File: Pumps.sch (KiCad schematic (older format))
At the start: 4 parts, among them Q1 TIP122

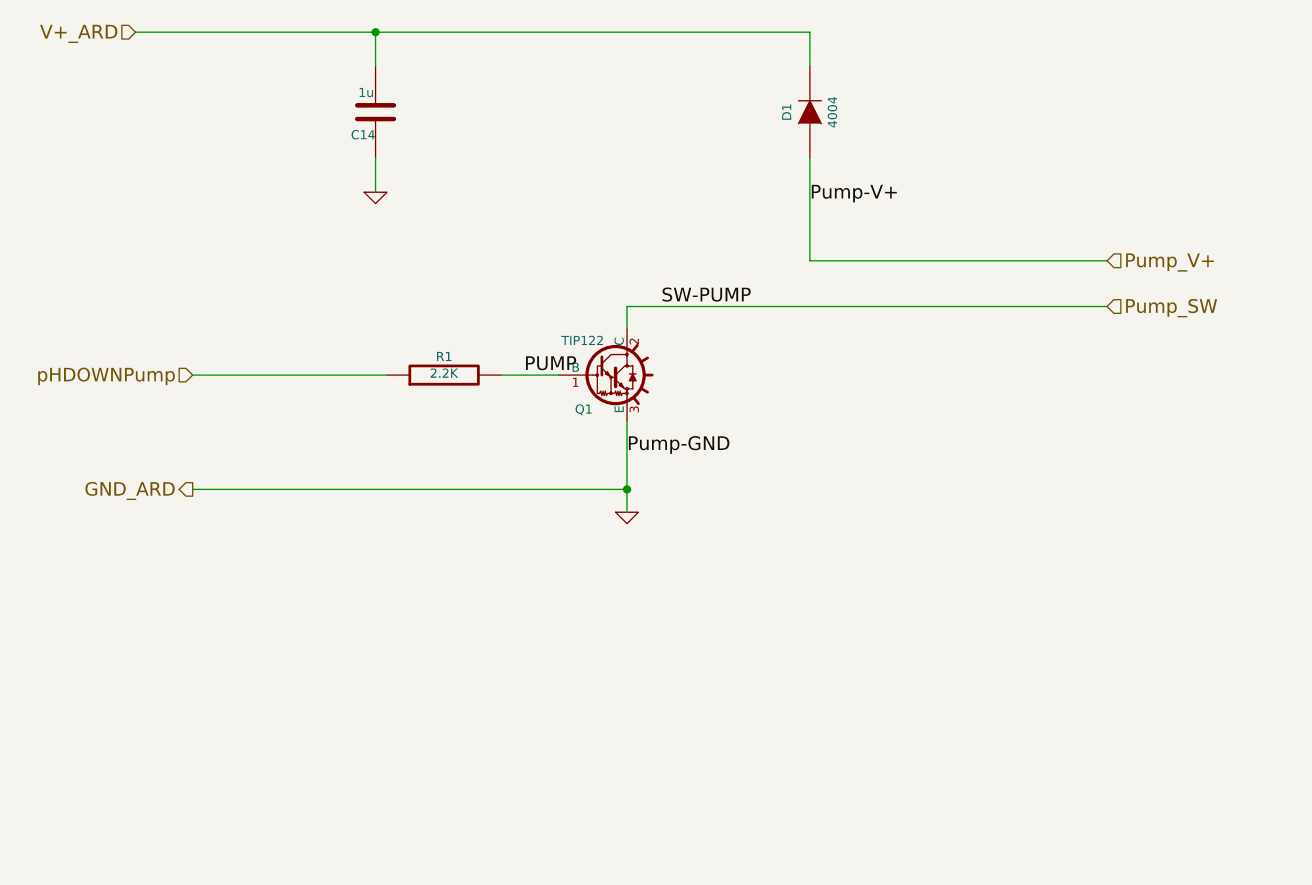
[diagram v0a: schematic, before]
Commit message: added 2nd pump in circuit to accomodate pH UP
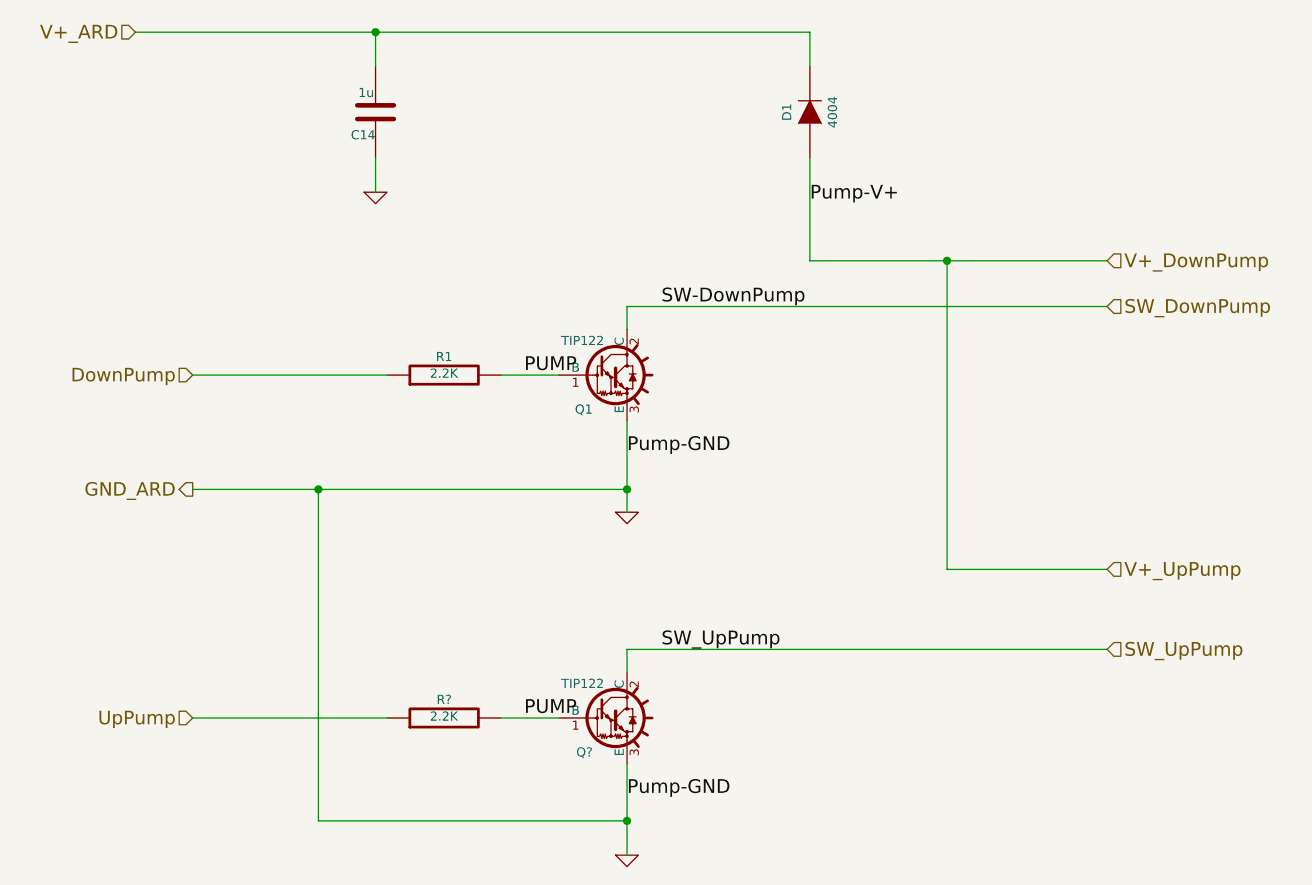
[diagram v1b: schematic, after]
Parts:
- added Q?: TIP122, TO220, symbol TIP120
- added R?: 2.2K, ~, symbol R
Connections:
- net GND: now also Q?.3 (E)
- net PUMP: now also Q?.1 (B), R?.2
- net Pump_SW renamed SW_DownPump
- net Pump_V+ renamed V+_DownPump
- net pHDOWNPump renamed DownPump
- new net SW_UpPump: Q?.2 (C)
- new net UpPump: R?.1
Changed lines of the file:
@@
 $Descr A4 11693 8268
 encoding utf-8
-Sheet 6 7
+Sheet 7 7
 Title ""
-Date "11 aug 2014"
+Date "12 aug 2014"
 Rev ""
 Comp ""
@@
 	4700 1150 4700 1300
 Text HLabel 2000 2650 0    59   Input ~ 0
-pHDOWNPump
+DownPump
 $Comp
 L GND #PWR12
@@
 	1750 1150 4700 1150
 Text Label 4050 2350 0    60   ~ 0
-SW-PUMP
+SW-DownPump
 Text Label 4700 1900 0    60   ~ 0
 Pump-V+
@@
 Pump-GND
 Text HLabel 6000 2150 2    60   Input ~ 0
-Pump_V+
+V+_DownPump
 Text HLabel 6000 2350 2    60   Input ~ 0
-Pump_SW
+SW_DownPump
+$Comp
+L TIP120 Q?
+U 1 1 53EA6E0F
+P 3800 4150
+F 0 "Q?" H 3750 4000 40  0000 R CNN
+F 1 "TIP122" H 3800 4300 40  0000 R CNN
+F 2 "TO220" H 3680 4255 29  0001 C CNN
+F 3 "~" H 3800 4150 60  0000 C CNN
+	1    3800 4150
+	1    0    0    -1
+$EndComp
+$Comp
+L R R?
+U 1 1 53EA6E15
+P 3100 4150
+F 0 "R?" V 3180 4150 40  0000 C CNN
+F 1 "2.2K" V 3107 4151 40  0000 C CNN
+F 2 "~" V 3030 4150 30  0000 C CNN
+F 3 "~" H 3100 4150 30  0000 C CNN
+	1    3100 4150
+	0    -1   -1   0
+$EndComp
+Wire Wire Line
+	3350 4150 3600 4150
+Wire Wire Line
+	2000 4150 2850 4150
+Text HLabel 2000 4150 0    59   Input ~ 0
+UpPump
+$Comp
+L GND #PWR?
+U 1 1 53EA6E1E
+P 3900 4750
+F 0 "#PWR?" H 3900 4750 30  0001 C CNN
+F 1 "GND" H 3900 4680 30  0001 C CNN
+F 2 "" H 3900 4750 60  0000 C CNN
+F 3 "" H 3900 4750 60  0000 C CNN
+	1    3900 4750
+	1    0    0    -1
+$EndComp
+Wire Wire Line
+	3900 3850 6000 3850
+Wire Wire Line
+	3900 3850 3900 3950
+Text Label 4050 3850 0    60   ~ 0
+SW_UpPump
+Text Label 3450 4150 0    60   ~ 0
+PUMP
+Wire Wire Line
+	3900 4350 3900 4750
+Text Label 3900 4500 0    60   ~ 0
+Pump-GND
+Text HLabel 6000 3850 2    60   Input ~ 0
+SW_UpPump
+Wire Wire Line
+	5300 2150 5300 3500
+Wire Wire Line
+	5300 3500 6000 3500
+Connection ~ 5300 2150
+Text HLabel 6000 3500 2    60   Input ~ 0
+V+_UpPump
+Wire Wire Line
+	2550 3150 2550 4600
+Wire Wire Line
+	2550 4600 3900 4600
+Connection ~ 3900 4600
+Connection ~ 2550 3150
 $EndSCHEMATC

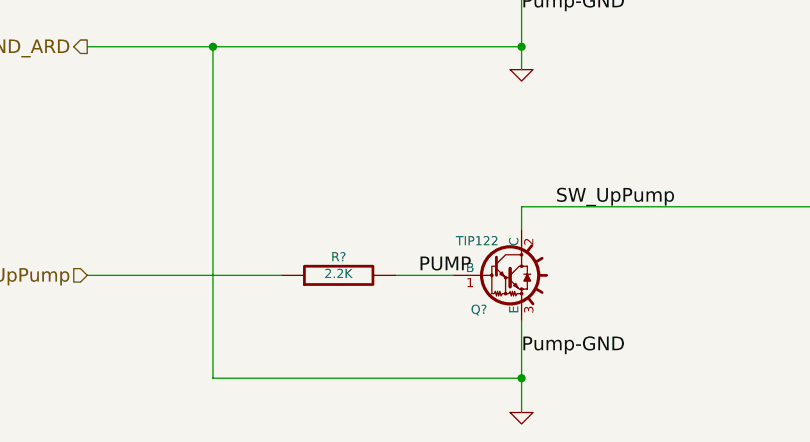
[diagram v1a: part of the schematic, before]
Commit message: changed op amp from LMV341 to MCP6241
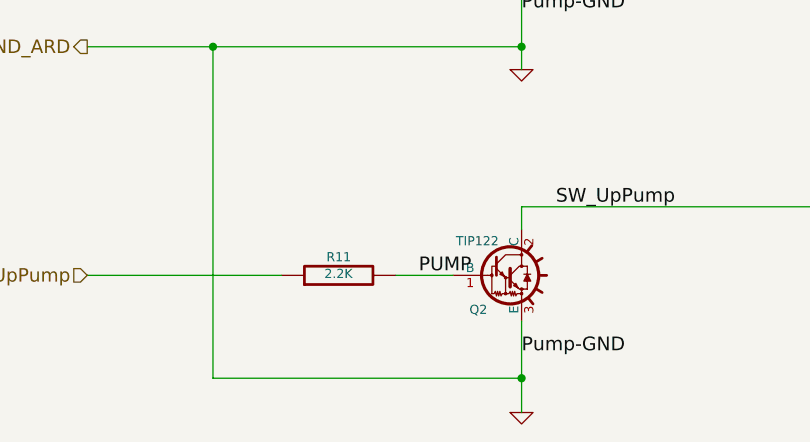
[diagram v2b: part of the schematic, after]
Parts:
- gave numbers to parts that had none: 2
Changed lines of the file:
@@
 Sheet 7 7
 Title ""
-Date "12 aug 2014"
+Date "14 aug 2014"
 Rev ""
 Comp ""
@@
 DownPump
 $Comp
-L GND #PWR12
+L GND #PWR13
 U 1 1 53DC3138
 P 3900 3250
-F 0 "#PWR12" H 3900 3250 30  0001 C CNN
+F 0 "#PWR13" H 3900 3250 30  0001 C CNN
 F 1 "GND" H 3900 3180 30  0001 C CNN
 F 2 "" H 3900 3250 60  0000 C CNN
@@
 Connection ~ 2800 1150
 $Comp
-L GND #PWR11
+L GND #PWR12
 U 1 1 53E3E3F6
 P 2800 1850
-F 0 "#PWR11" H 2800 1850 30  0001 C CNN
+F 0 "#PWR12" H 2800 1850 30  0001 C CNN
 F 1 "GND" H 2800 1780 30  0001 C CNN
 F 2 "" H 2800 1850 60  0000 C CNN
@@
 SW_DownPump
 $Comp
-L TIP120 Q?
+L TIP120 Q2
 U 1 1 53EA6E0F
 P 3800 4150
-F 0 "Q?" H 3750 4000 40  0000 R CNN
+F 0 "Q2" H 3750 4000 40  0000 R CNN
 F 1 "TIP122" H 3800 4300 40  0000 R CNN
 F 2 "TO220" H 3680 4255 29  0001 C CNN
@@
 $EndComp
 $Comp
-L R R?
+L R R11
 U 1 1 53EA6E15
 P 3100 4150
-F 0 "R?" V 3180 4150 40  0000 C CNN
+F 0 "R11" V 3180 4150 40  0000 C CNN
 F 1 "2.2K" V 3107 4151 40  0000 C CNN
 F 2 "~" V 3030 4150 30  0000 C CNN
@@
 UpPump
 $Comp
-L GND #PWR?
+L GND #PWR14
 U 1 1 53EA6E1E
 P 3900 4750
-F 0 "#PWR?" H 3900 4750 30  0001 C CNN
+F 0 "#PWR14" H 3900 4750 30  0001 C CNN
 F 1 "GND" H 3900 4680 30  0001 C CNN
 F 2 "" H 3900 4750 60  0000 C CNN
